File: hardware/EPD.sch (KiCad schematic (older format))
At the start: 0 parts

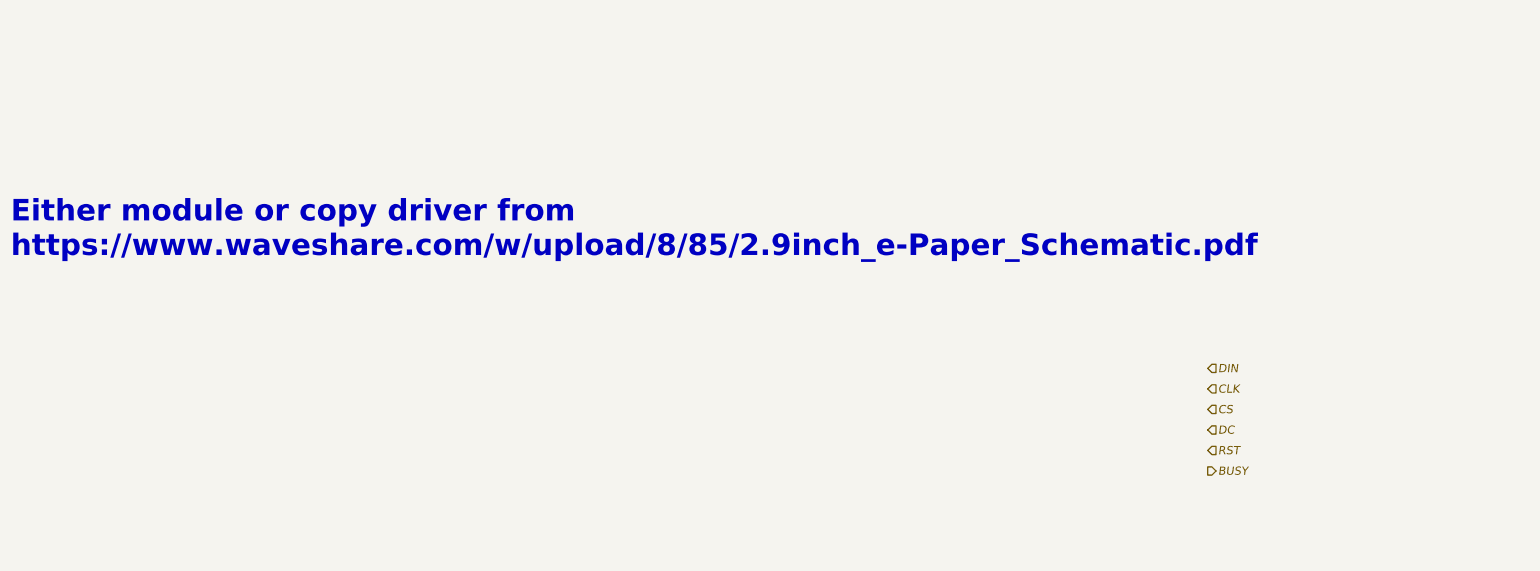
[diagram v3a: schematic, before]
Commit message: Added SPI connection for EPD
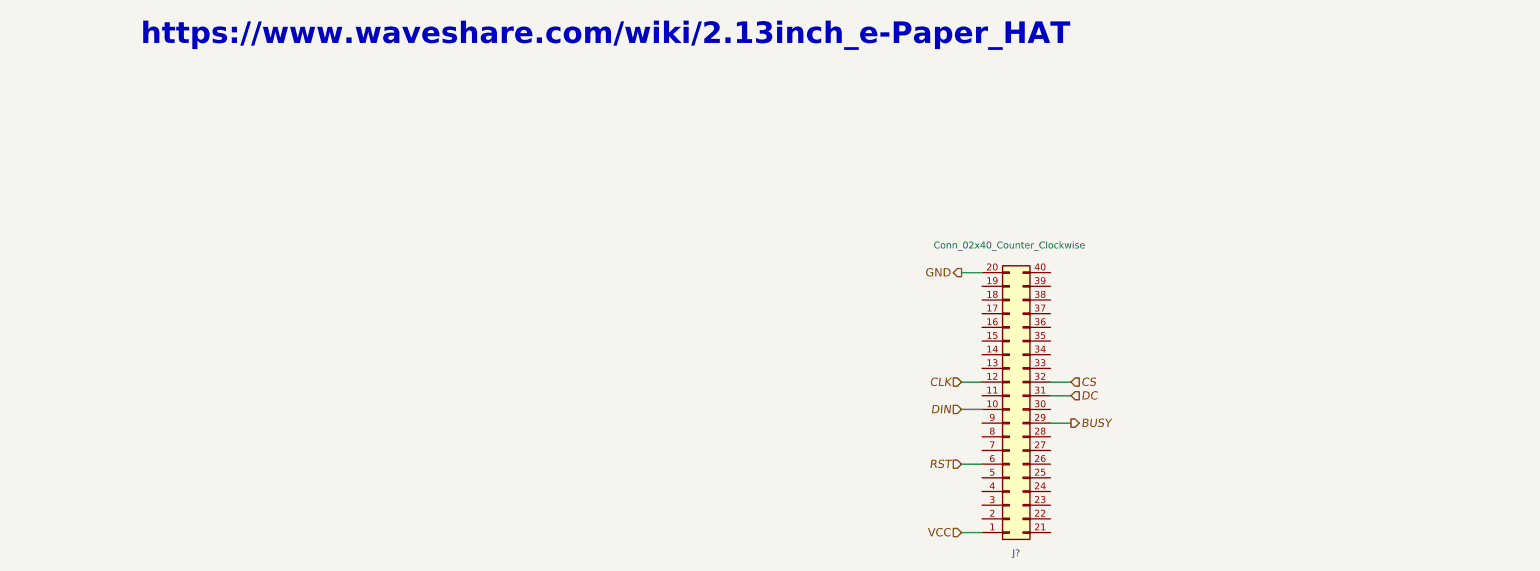
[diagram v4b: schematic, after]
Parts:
- added J?: Conn_02x40_Counter_Clockwise, symbol Conn_02x20_Top_Bottom
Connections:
- net BUSY: now also J?.29 (Pin_29)
- net CLK: now also J?.12 (Pin_12)
- net CS: now also J?.32 (Pin_32)
- net DC: now also J?.31 (Pin_31)
- net DIN: now also J?.10 (Pin_10)
- net RST: now also J?.6 (Pin_6)
- new net GND: J?.20 (Pin_20)
- new net VCC: J?.1 (Pin_1)
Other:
- note added: "https://www.waveshare.com/wiki/2.13inch_e-Paper_HAT"
- note removed: "Either module or copy driver from\nhttps://www.waveshare.com/w/upload/8/85/2.9inch_e-Paper_Schematic.pdf"
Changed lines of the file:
@@
 $Descr A4 11693 8268
 encoding utf-8
-Sheet 4 5
+Sheet 2 5
 Title "IoT conference badge - mainboard"
 Date ""
@@
 Comment4 ""
 $EndDescr
-Text Notes 1350 2500 0    157  ~ 31
-Either module or copy driver from\nhttps://www.waveshare.com/w/upload/8/85/2.9inch_e-Paper_Schematic.pdf
-Text HLabel 10100 3300 2    60   Input Italic 0
+Text Notes 2300 950  0    157  ~ 31
+https://www.waveshare.com/wiki/2.13inch_e-Paper_HAT
+Text HLabel 8300 3600 0    60   Input Italic 0
 DIN
-Text HLabel 10100 3450 2    60   Input Italic 0
+Text HLabel 8300 3400 0    60   Input Italic 0
 CLK
-Text HLabel 10100 3600 2    60   Input Italic 0
+Text HLabel 9100 3400 2    60   Input Italic 0
 CS
-Text HLabel 10100 3750 2    60   Input Italic 0
+Text HLabel 9100 3500 2    60   Input Italic 0
 DC
-Text HLabel 10100 3900 2    60   Input Italic 0
+Text HLabel 8300 4000 0    60   Input Italic 0
 RST
-Text HLabel 10100 4050 2    60   Output Italic 0
+Text HLabel 9100 3700 2    60   Output Italic 0
 BUSY
+Text HLabel 8300 2600 0    60   Output ~ 0
+GND
+Text HLabel 8300 4500 0    60   Input ~ 0
+VCC
+$Comp
+L Conn_02x20_Top_Bottom J?
+U 1 1 5AFF86AB
+P 8650 3600
+F 0 "J?" H 8700 4650 50  0000 C CNN
+F 1 "Conn_02x40_Counter_Clockwise" H 8650 2400 50  0000 C CNN
+F 2 "" H 8650 3600 50  0001 C CNN
+F 3 "" H 8650 3600 50  0001 C CNN
+	1    8650 3600
+	1    0    0    1
+$EndComp
+Wire Wire Line
+	8300 4500 8450 4500
+Wire Wire Line
+	8300 2600 8450 2600
+Wire Wire Line
+	8300 4000 8450 4000
+Wire Wire Line
+	8300 3600 8450 3600
+Wire Wire Line
+	8300 3400 8450 3400
+Wire Wire Line
+	9100 3700 8950 3700
+Wire Wire Line
+	9100 3500 8950 3500
+Wire Wire Line
+	9100 3400 8950 3400
 $EndSCHEMATC
